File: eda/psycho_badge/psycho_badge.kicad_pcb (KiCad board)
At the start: 2 copper layers, 0 parts

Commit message: psycho badge art and eda updates
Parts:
- added REF**: GC9A01_TFT, 0_local:GC9A01_TFT, F.Cu at (195.0, 111.0)
- added REF**: Rectangle_4x6, 0_badge:Rectangle_4x6, F.Cu at (140.5, 85.7)
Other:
- board outline added: 152.4 x 101.6 mm

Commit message: pre dc33 updates
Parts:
- removed the REF** at (195.0, 111.0)
- added REF**: TFT_LCD_ST7735S_MSP1443_SPI_1_44IN_RearMnt, 0_local:TFT_LCD_ST7735S_MSP1443_SPI_1_44IN_RearMnt, F.Cu at (142.6, 109.5)
- added REF**: ESP32_WEMOS_LOLIN32_LITE_back, 0_local:ESP32_WEMOS_LOLIN32_LITE_back, F.Cu at (184.5, 85.6)
- moved REF** 4.00 mm to (140.5, 81.7)

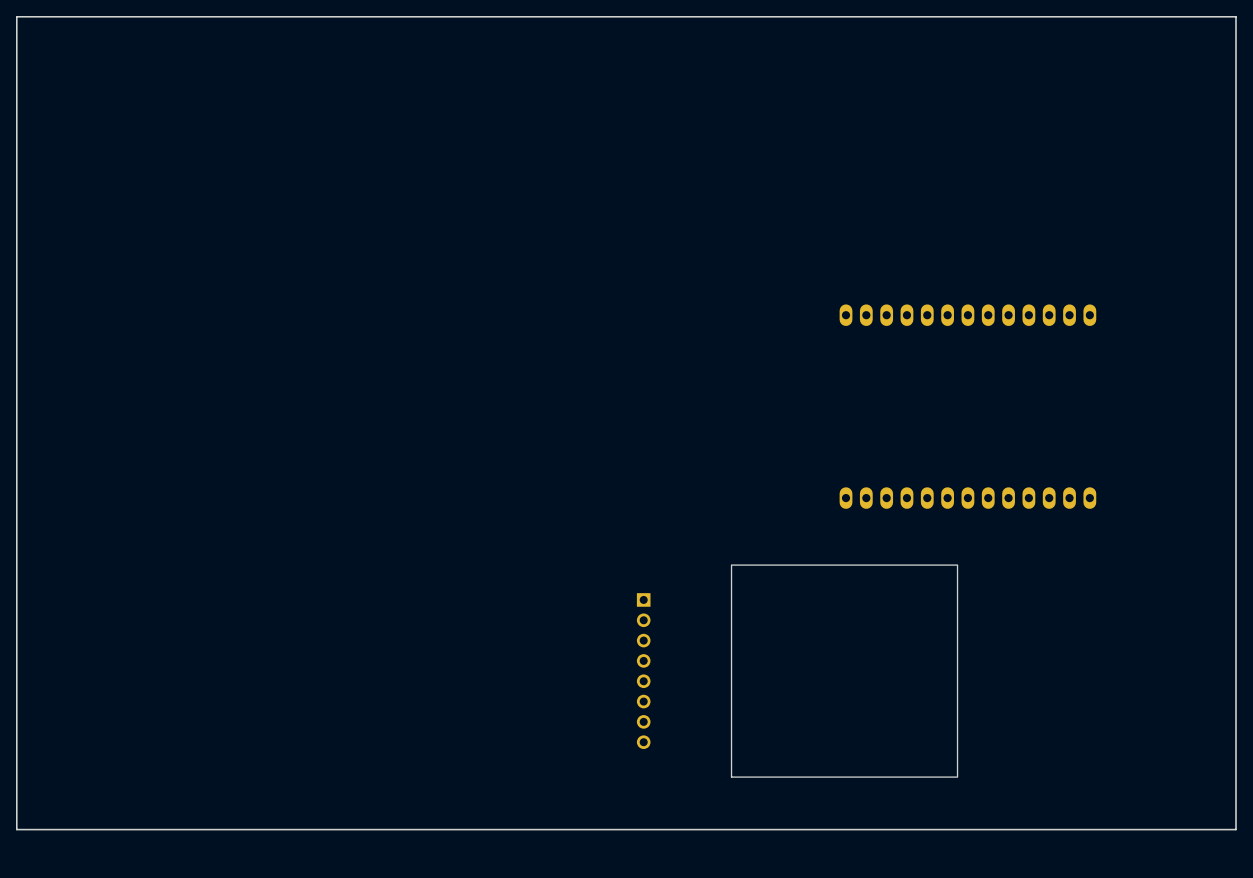
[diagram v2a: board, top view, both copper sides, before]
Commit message: added eink display circuit and dev board
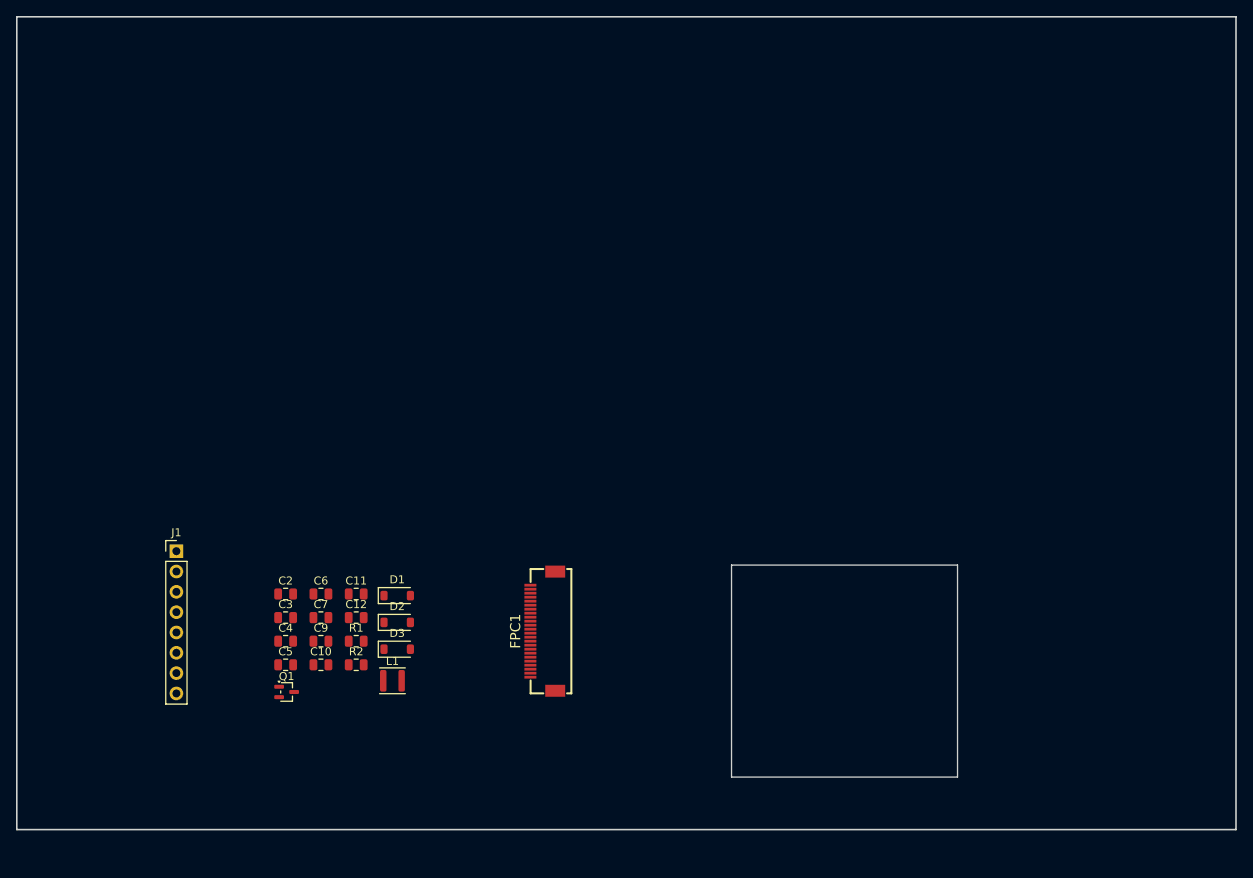
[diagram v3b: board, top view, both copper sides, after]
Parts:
- removed the REF** at (142.6, 109.5)
- removed the REF** at (184.5, 85.6)
- added C10: 1uF, 0_local:C_0805_2012Metric, F.Cu at (102.3, 117.7)
- added C11: 1uF, 0_local:C_0805_2012Metric, F.Cu at (106.7, 108.8)
- added C12: 1uF, 0_local:C_0805_2012Metric, F.Cu at (106.7, 111.8)
- added C2: 1uF, 0_local:C_0805_2012Metric, F.Cu at (97.9, 108.8)
- added C3: 4.7uF, 0_local:C_0805_2012Metric, F.Cu at (97.9, 111.8)
- added C4: 4.7uF, 0_local:C_0805_2012Metric, F.Cu at (97.9, 114.8)
- added C5: 1uF, 0_local:C_0805_2012Metric, F.Cu at (97.9, 117.7)
- added C6: 1uF, 0_local:C_0805_2012Metric, F.Cu at (102.3, 108.8)
- added C7: 1uF, 0_local:C_0805_2012Metric, F.Cu at (102.3, 111.8)
- added C9: 1uF, 0_local:C_0805_2012Metric, F.Cu at (102.3, 114.8)
- added D1: MBR0530, 0_local:D_SOD-123, F.Cu at (111.8, 109.0)
- added D2: MBR0530, 0_local:D_SOD-123, F.Cu at (111.8, 112.4)
- added D3: MBR0530, 0_local:D_SOD-123, F.Cu at (111.8, 115.8)
- added FPC1: FPC05-H0.5-24AH2.0, 0_local:FPC-SMD_24P-P0.50_FPC05-H0.5-24AH2.0, F.Cu at (130.0, 113.5)
- added J1: Conn_01x08, 0_local:Conn_Pin_Header_Straight_1x08_Pitch2.54mm, F.Cu at (84.2, 103.5)
- added L1: 47uH, 0_local:L_APV_ANR3015, F.Cu at (111.3, 119.7)
- added Q1: Si1308EDL, 0_local:SOT-323_SC-70, F.Cu at (98.0, 121.1)
- added R1: 1M, 0_local:R_0805_2012Metric, F.Cu at (106.7, 114.8)
- added R2: 2.2, 0_local:R_0805_2012Metric, F.Cu at (106.7, 117.7)

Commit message: art updates
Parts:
- removed C10, C11, C12, C2, C5, C6, C7, C9: 1uF, 0_local:C_0805_2012Metric
- removed C3, C4: 4.7uF, 0_local:C_0805_2012Metric
- removed D1, D2, D3: MBR0530, 0_local:D_SOD-123
- removed FPC1: FPC05-H0.5-24AH2.0, 0_local:FPC-SMD_24P-P0.50_FPC05-H0.5-24AH2.0
- removed J1: Conn_01x08, 0_local:Conn_Pin_Header_Straight_1x08_Pitch2.54mm
- removed L1: 47uH, 0_local:L_APV_ANR3015
- removed Q1: Si1308EDL, 0_local:SOT-323_SC-70
- removed R1: 1M, 0_local:R_0805_2012Metric
- removed R2: 2.2, 0_local:R_0805_2012Metric
- added G***: LOGO, 0_badge:psycho_badge_top_art, F.Cu at (140.5, 87.5)

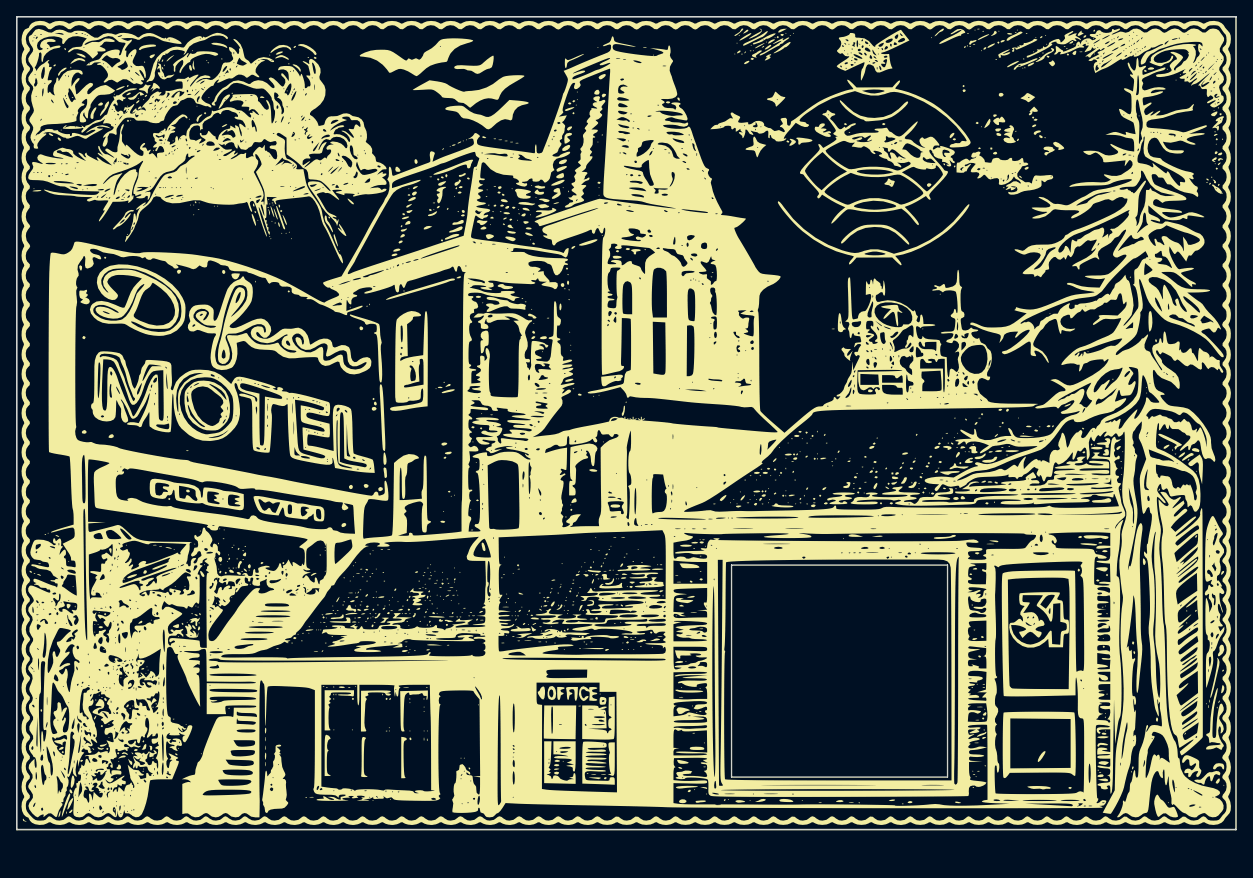
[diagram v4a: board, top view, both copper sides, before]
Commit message: component layout done
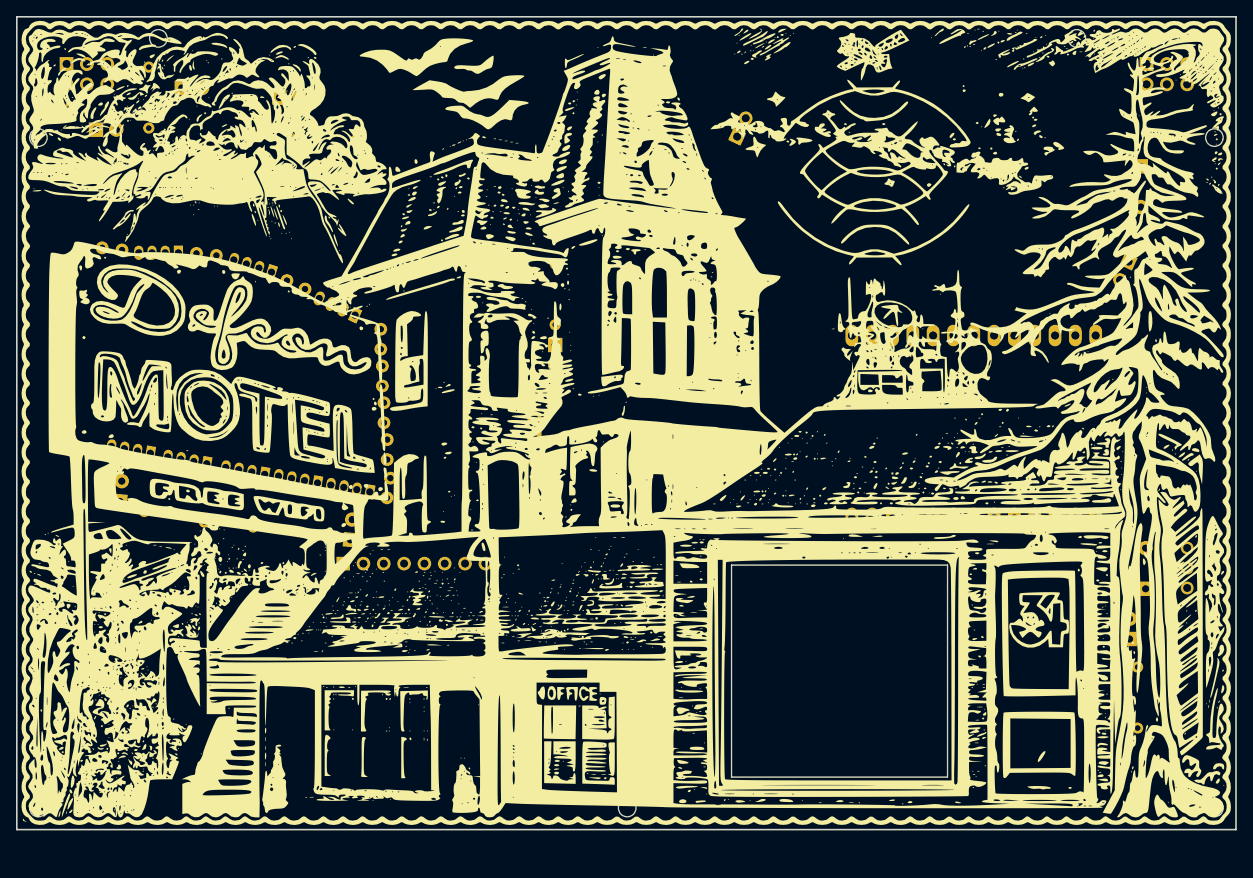
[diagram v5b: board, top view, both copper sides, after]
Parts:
- added BT1: Battery_Lipo, 0_local:Battery_Connector_back, F.Cu at (204.8, 55.4)
- added C10: C_Disc_D3, 0_local:C_Disc_D3_back, F.Cu at (75.0, 65.6)
- added C11: C_Disc_D3, 0_local:C_Disc_D3_back, F.Cu at (86.8, 66.3)
- added C12: C_Disc_D3, 0_local:C_Disc_D3_back, F.Cu at (98.1, 69.7)
- added C20: C_Disc_D3, 0_local:C_Disc_D3_back, F.Cu at (109.8, 75.8)
- added C21: C_Disc_D3, 0_local:C_Disc_D3_back, F.Cu at (110.0, 80.3)
- added C22: C_Disc_D3, 0_local:C_Disc_D3_back, F.Cu at (110.2, 85.0)
- added C23: C_Disc_D3, 0_local:C_Disc_D3_back, F.Cu at (110.6, 89.5)
- added C24: C_Disc_D3, 0_local:C_Disc_D3_back, F.Cu at (111.0, 94.4)
- added D1: LED_3mm, 0_local:LED_D3.0mm-2-std_back, F.Cu at (77.2, 97.3)
- added D10: LED_WS2812D_5mm, 0_local:LED_D5.0mm-4_WS2812D_2024_back, F.Cu at (84.0, 66.2)
- added D11: LED_WS2812D_5mm, 0_local:LED_D5.0mm-4_WS2812D_2024_back, F.Cu at (95.7, 68.5)
- added D12: LED_WS2812D_5mm, 0_local:LED_D5.0mm-4_WS2812D_2024_back, F.Cu at (106.1, 73.8)
- added D2: LED_3mm, 0_local:LED_D3.0mm-2-std_back, F.Cu at (106.0, 102.1)
- added D20: LED_WS2812D_5mm, 0_local:LED_D5.0mm-4_WS2812D_2024_back, F.Cu at (80.5, 91.2)
- added D21: LED_WS2812D_5mm, 0_local:LED_D5.0mm-4_WS2812D_2024_back, F.Cu at (87.6, 92.5)
- added D22: LED_WS2812D_5mm, 0_local:LED_D5.0mm-4_WS2812D_2024_back, F.Cu at (94.8, 93.8)
- added D23: LED_WS2812D_5mm, 0_local:LED_D5.0mm-4_WS2812D_2024_back, F.Cu at (101.4, 94.9)
- added D24: LED_WS2812D_5mm, 0_local:LED_D5.0mm-4_WS2812D_2024_back, F.Cu at (107.9, 96.0)
- added D31: LED_3mm, 0_local:LED_D3.0mm-2-std_back, F.Cu at (74.2, 50.8)
- added D32: LED_3mm, 0_local:LED_D3.0mm-2-std_back, F.Cu at (97.1, 46.8)
- added D4: LED_3mm, 0_local:LED_D3.0mm-2-std_back, F.Cu at (84.9, 45.6)
- added D51: LED_3mm, 0_local:LED_D3.0mm-2-std_back, F.Cu at (129.0, 89.4)
- added D52: LED_3mm, 0_local:LED_D3.0mm-2-std_back, F.Cu at (131.6, 77.7)
- added D6: LED_3mm, 0_local:LED_D3.0mm-2-std_back, F.Cu at (203.4, 114.5)
- added DS1: GDEM0154F51H_EINK_DEV, 0_local:GDEM0154F51H_EINK_DEV_TFT, F.Cu at (134.3, 127.8)
- added J1: Battery_Conn, 0_local:Battery_Connector_back, F.Cu at (205.4, 108.2)
- added J21: 01x02, 0_local:Conn_Pin_Header_Male_Horiz_Back_1x02_Pitch2.54mm, F.Cu at (203.3, 67.3)
- added J22: 01x02, 0_local:Conn_Pin_Header_Male_Horiz_Back_1x02_Pitch2.54mm, F.Cu at (154.3, 51.7)
- added JSAO1: Conn_02x03_SAO, 0_sao_v169bis:SAOv169-BADGEv2b-PO-2x3, F.Cu at (208.0, 43.9)
- added JSAO2: Conn_02x03_SAO, 0_sao_v169bis:SAOv169-BADGEv2b-PO-2x3, F.Cu at (73.0, 43.9)
- added R1: 47R_6.3mm, 0_local:R_Axial_DIN0207_L6.3_D2.5_P7.62_Horiz_back, F.Cu at (80.2, 98.5)
- added R10: 47R_6.3mm, 0_local:R_Axial_DIN0207_L6.3_D2.5_P7.62_Horiz_back, F.Cu at (70.0, 68.0)
- added R2: 47R_6.3mm, 0_local:R_Axial_DIN0207_L6.3_D2.5_P7.62_Horiz_back, F.Cu at (101.4, 101.8)
- added R20: 47R_6.3mm, 0_local:R_Axial_DIN0207_L6.3_D2.5_P7.62_Horiz_back, F.Cu at (70.0, 87.0)
- added R31: 47R_6.3mm, 0_local:R_Axial_DIN0207_L6.3_D2.5_P7.62_Horiz_back, F.Cu at (71.0, 55.6)
- added R32: 47R_6.3mm, 0_local:R_Axial_DIN0207_L6.3_D2.5_P7.62_Horiz_back, F.Cu at (99.2, 52.0)
- added R4: 47R_6.3mm, 0_local:R_Axial_DIN0207_L6.3_D2.5_P7.62_Horiz_back, F.Cu at (80.8, 43.0)
- added R51: 47R_6.3mm, 0_local:R_Axial_DIN0207_L6.3_D2.5_P7.62_Horiz_back, F.Cu at (129.0, 92.4)
- added R52: 47R_6.3mm, 0_local:R_Axial_DIN0207_L6.3_D2.5_P7.62_Horiz_back, F.Cu at (131.6, 75.2)
- added R6: 47R_6.3mm, 0_local:R_Axial_DIN0207_L6.3_D2.5_P7.62_Horiz_back, F.Cu at (204.4, 118.0)
- added REF**: MountingHole_2.2mm_M2, 0_local:MountingHole_2.2mm_M2, F.Cu at (214.0, 51.8)
- added REF**: Battery_LIPO_103040_silk_back, 0_local:Battery_LIPO_103040_silk_back, F.Cu at (178.4, 56.8)
- added REF**: MountingHole_2.2mm_M2, 0_local:MountingHole_2.2mm_M2, F.Cu at (196.8, 39.4)
- added REF**: MountingHole_2.2mm_M2, 0_local:MountingHole_2.2mm_M2, F.Cu at (82.0, 39.4)
- added REF**: MountingHole_2.2mm_M2, 0_local:MountingHole_2.2mm_M2, F.Cu at (67.0, 51.8)
- added REF**: MountingHole_2.2mm_M2, 0_local:MountingHole_2.2mm_M2, F.Cu at (140.6, 135.6)
- added REF**: MountingHole_2.2mm_M2, 0_local:MountingHole_2.2mm_M2, F.Cu at (214.0, 135.6)
- added REF**: MountingHole_2.2mm_M2, 0_local:MountingHole_2.2mm_M2, F.Cu at (67.0, 135.6)
- added SW1: SW_SPDT_SS12D00G, 0_local:SW_SPDT_Slide_SS12D00G-1P2T_3pin_back, F.Cu at (210.6, 105.6)
- added U1: ESP32-WEMOS-LOLIN32-LITE, 0_local:ESP32_WEMOS_LOLIN32_LITE_back, F.Cu at (185.2, 88.1)

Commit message: pcb tracing
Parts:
- moved C22 41.1 mm to (72.0, 100.2)
- moved R20 40.9 mm to (110.5, 92.7), turned to 95 degrees
- moved R10 39.7 mm to (109.0, 75.4), turned to -85 degrees
- moved C24 39.2 mm to (72.0, 90.7), turned to -90 degrees
- moved C23 39.0 mm to (72.0, 95.4)
- moved D24 32.0 mm to (76.4, 90.3), turned to -10 degrees
- moved D12 28.6 mm to (78.6, 65.8), turned to 0 degrees
- moved C12 25.5 mm to (72.9, 65.4), turned to -6 degrees
- moved D20 24.5 mm to (104.6, 95.2), turned to -10 degrees
- moved C20 24.2 mm to (111.0, 100.0), turned to 90 degrees
- moved C10 23.3 mm to (97.9, 69.7), turned to -25 degrees
- moved C21 22.0 mm to (105.8, 101.9), turned to 0 degrees
- moved D10 19.8 mm to (103.0, 71.8), turned to -25 degrees
- moved D23 17.6 mm to (84.1, 91.5), turned to -10 degrees
- moved R4 15.7 mm to (85.1, 58.1), turned to 0 degrees
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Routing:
- net 23: track 0.00 -> 70.4 mm
- net 18: track 0.00 -> 70.1 mm
- net 5: track 0.00 -> 70.0 mm
- net 17: track 0.00 -> 69.6 mm
- net 16: track 0.00 -> 69.5 mm
- net Net-(BT1-Pin_1): track 0.00 -> 53.2 mm
- net GBAT: track 0.00 -> 44.4 mm
- net 12: track 0.00 -> 38.9 mm
- net Net-(D32-K): track 0.00 -> 8.54 mm
- net Net-(D31-K): track 0.00 -> 7.30 mm
- net Net-(D4-K): track 0.00 -> 6.08 mm
- net VBAT: track 0.00 -> 5.24 mm
- net Net-(D51-K): track 0.00 -> 2.99 mm
- net Net-(D6-K): track 0.00 -> 2.56 mm
- net Net-(D52-K): track 0.00 -> 2.52 mm
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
